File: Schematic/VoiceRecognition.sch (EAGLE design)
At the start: 28 parts, among them Q1 16MHz, X1 USB-A

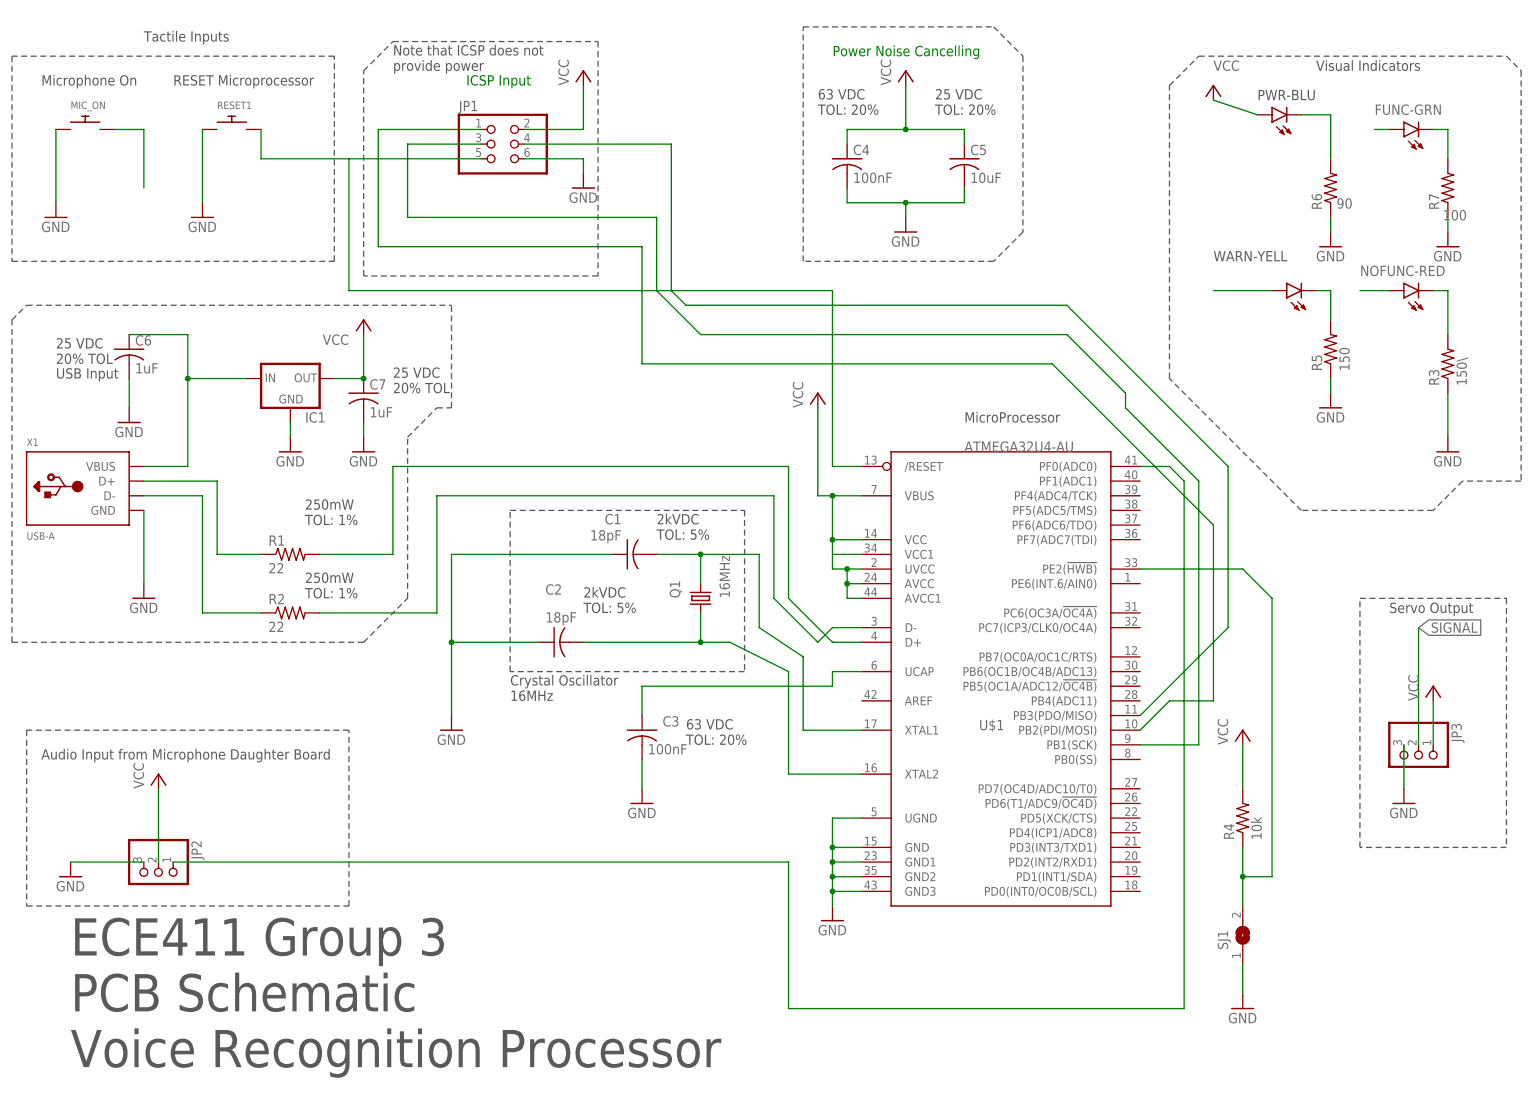
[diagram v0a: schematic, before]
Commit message: PCB Schematic completed
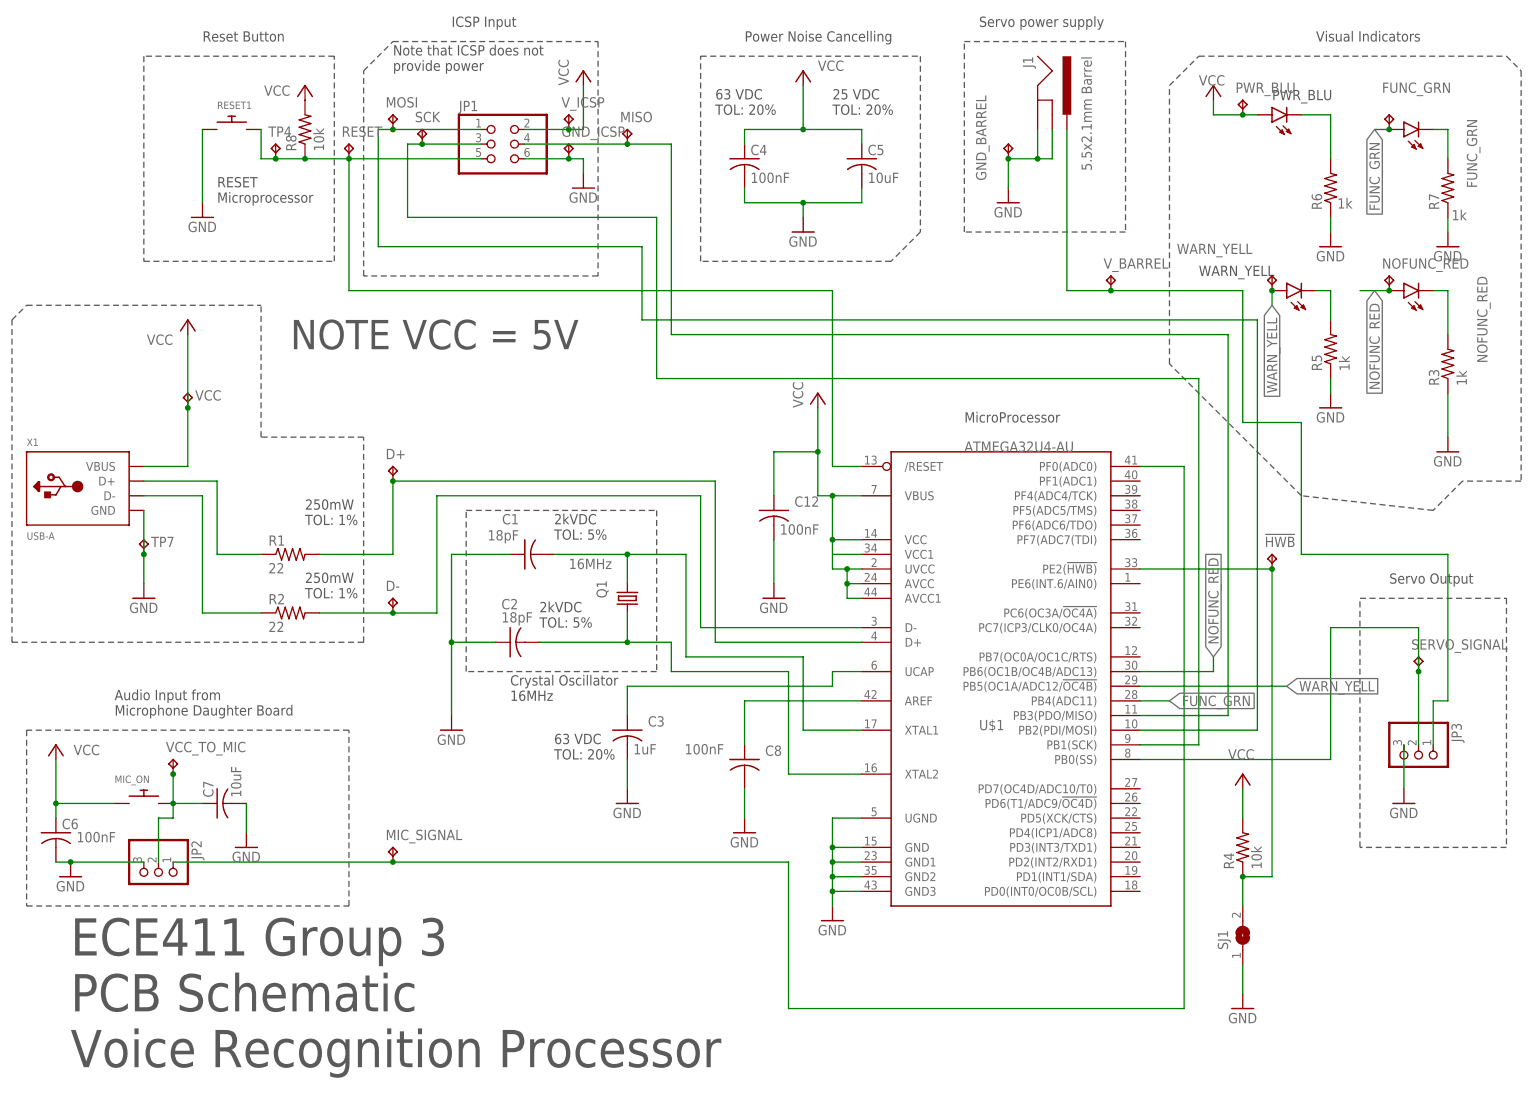
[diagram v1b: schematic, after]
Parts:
- removed IC1: (no value), adafruit:MCP1700INLINE
- added !HWB, D+, D-, FUNC_GRN, GND_BARREL, GND_ICSP, MIC_SIGNAL, MISO, MOSI, NOFUNC_RED, PWR_BLU, RESET, SCK, SERVO_SIGNAL, TP4, TP7, VCC, VCC_TO_MIC, V_BARREL, V_ICSP, WARN_YELL: TPTP15SQ, testpad:TPTP15SQ
- added C12, C8: 100nF, rcl:C-USC1206
- added J1: 5.5x2.1mm Barrel, SparkFun-Connectors:POWER_JACKSMD
- added R8: 10k, rcl:R-US_M1206
- C3: value 100nF -> 1uF
- C6: value 1uF -> 100nF
- C7: value 1uF -> 10uF
- R3: value 150\ -> 1k
- R5: value 150 -> 1k
- R6: value 90 -> 1k
- R7: value 100 -> 1k
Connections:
- removed net FUNC-GRN: LED2.A
- removed net N$10: C6.1, IC1.IN, X1.VBUS
- removed net N$11: MIC_ON.P$2
- removed net N$4: JP1.3, U$1.PB1(SCK)
- removed net NOFUNC-RED: LED3.A
- removed net WARN: LED4.A
- new net FUNC_GRN: FUNC_GRN.TP, LED2.A, U$1.PB4(ADC11)
- new net MIC_SIGNAL: JP2.1, MIC_SIGNAL.TP, U$1.PF0(ADC0)
- new net N$14: C8.1, U$1.AREF
- new net N$20: D-.TP, R2.2, U$1.D-
- new net NOFUNC_RED: LED3.A, NOFUNC_RED.TP, U$1.PB6(OC1B/OC4B/ADC13)
- new net SERVO_POS: J1.PWR, JP3.1, V_BARREL.TP
- new net WARN_YELL: LED4.A, U$1.PB5(OC1A/ADC12/!OC4B), WARN_YELL.TP
- net GND: now also C12.2, C8.2, GND_BARREL.TP, GND_ICSP.TP, J1.GND, J1.GNDBREAK, TP7.TP; no longer IC1.GND, MIC_ON.P$1
- net HWB: now also !HWB.TP
- net N$12: now also D+.TP
- net N$13: now also MOSI.TP
- net N$15: now also C7.1, JP2.2, MIC_ON.P$2, VCC_TO_MIC.TP; no longer JP2.1, U$1.PF0(ADC0)
- net N$17: now also MISO.TP
- net N$2: now also JP1.3, SCK.TP, U$1.PB1(SCK); no longer R2.2, U$1.D-
- net RST: now also R8.1, RESET.TP, TP4.TP
- net SIGNAL: now also SERVO_SIGNAL.TP, U$1.PB0(SS)
- net VCC: now also C12.1, C6.1, MIC_ON.P$1, PWR_BLU.TP, R8.2, VCC.TP, V_ICSP.TP, X1.VBUS; no longer C7.1, IC1.OUT, JP2.2, JP3.1
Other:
- note added: "NOTE VCC = 5V"
- note added: "PWR_BLU"
- note added: "Reset Button"
- note added: "Servo power supply"
- note added: "WARN_YELL"
- note removed: "25 VDC 20% TOL"
- note removed: "Microphone On"
- note removed: "PWR-BLU"
- note removed: "Tactile Inputs"
- note removed: "USB Input"
- note removed: "WARN-YELL"
- moved on the sheet: C1, C2, C3, C4, C5, C6, C7, MIC_ON, Q1, R4
